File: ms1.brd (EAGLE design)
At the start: 100 x 100 mm, 123 parts, among them IC1 MAX3232EUE, J1 POWERPOLE_POWER25A, J10 RS485, J11 I2C, J12 TTL_SERIAL, J13 Radio, J14 RS232, J2 RAIN, J3 ADC1, J4 ON, J5 D1, J6 D2, J7 ADC2, J8 LED-EN, Q1 DMG6602SVT, Q2 DMG6602SVT, Q3 DMG6602SVT, Q4 DMG6602SVT, U1 LT1934ES6TRMPBF, U2 LT1934ES6TRMPBF, U3 DS3231SN, U4 ISL3179EIBZ, X1 KUSBVX-BS1N

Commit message: As submitted to hackvana
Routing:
- net RS485_P: track 18.1 -> 10.8 mm, vias 0 -> 1
- net RS485_N: track 17.7 -> 10.5 mm
- net GND: vias 18 -> 21
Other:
- board text added: "GMB"
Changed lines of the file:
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@@
 <setting verticaltext="up"/>
 </settings>
-<grid distance="5" unitdist="mil" unit="mil" style="lines" multiple="1" display="yes" altdistance="1" altunitdist="mil" altunit="mil"/>
+<grid distance="20" unitdist="mil" unit="mil" style="lines" multiple="1" display="yes" altdistance="1" altunitdist="mil" altunit="mil"/>
 <layers>
 <layer number="1" name="Top" color="4" fill="1" visible="yes" active="yes"/>
@@
 <text x="2.794" y="0.381" size="1.778" layer="25">PJB</text>
 <text x="9.652" y="0.254" size="1.778" layer="25">TW</text>
+<text x="14.859" y="0.254" size="1.778" layer="25">GMB</text>
 </plain>
 <attributes>
@@
 </class>
 <class number="2" name="rs485" width="0.3048" drill="0.3556">
-<clearance class="2" value="0.1524"/>
+<clearance class="2" value="0.3048"/>
 </class>
 </classes>
-<designrules name="Hackvana">
+<designrules name="Hackvana *">
 <description language="de">&lt;b&gt;EAGLE Design Rules&lt;/b&gt;
 &lt;p&gt;
@@
 <param name="mlMinStopFrame" value="2mil"/>
 <param name="mlMaxStopFrame" value="2mil"/>
-<param name="mlMinCreamFrame" value="0mil"/>
-<param name="mlMaxCreamFrame" value="0mil"/>
+<param name="mlMinCreamFrame" value="0.15mm"/>
+<param name="mlMaxCreamFrame" value="0.15mm"/>
 <param name="mlViaStopLimit" value="100mil"/>
 <param name="srRoundness" value="0"/>
@@
 <via x="6.604" y="33.528" extent="1-16" drill="0.4826" shape="square"/>
 <via x="64.897" y="18.161" extent="1-16" drill="0.4826" shape="square"/>
+<via x="61.976" y="32.385" extent="1-16" drill="0.4826" shape="square"/>
+<via x="87.503" y="76.581" extent="1-16" drill="0.4826" shape="square"/>
+<via x="67.691" y="86.995" extent="1-16" drill="0.4826" shape="square"/>
 </signal>
 <signal name="VCC">
@@
 <via x="11.303" y="2.667" extent="1-16" drill="0.6" shape="square"/>
 <via x="47.244" y="2.667" extent="1-16" drill="0.6" shape="square"/>
-<via x="48.514" y="34.163" extent="1-16" drill="0.6" shape="square"/>
+<via x="48.514" y="33.655" extent="1-16" drill="0.6" shape="square"/>
 <via x="10.795" y="37.465" extent="1-16" drill="0.6" shape="square"/>
 <via x="41.021" y="10.287" extent="1-16" drill="0.6" shape="square"/>
 <via x="17.145" y="18.796" extent="1-16" drill="0.6" shape="square"/>
+<via x="26.035" y="37.465" extent="1-16" drill="0.6" shape="square"/>
+<via x="33.655" y="37.465" extent="1-16" drill="0.6" shape="square"/>
+<via x="18.415" y="33.655" extent="1-16" drill="0.6" shape="square"/>
+<via x="26.035" y="33.655" extent="1-16" drill="0.6" shape="square"/>
+<via x="33.655" y="33.655" extent="1-16" drill="0.6" shape="square"/>
+<via x="45.085" y="33.655" extent="1-16" drill="0.6" shape="square"/>
+<via x="22.225" y="22.225" extent="1-16" drill="0.6" shape="square"/>
+<via x="29.845" y="22.225" extent="1-16" drill="0.6" shape="square"/>
+<via x="37.465" y="22.225" extent="1-16" drill="0.6" shape="square"/>
+<via x="22.225" y="18.415" extent="1-16" drill="0.6" shape="square"/>
+<via x="29.845" y="18.415" extent="1-16" drill="0.6" shape="square"/>
+<via x="37.465" y="18.415" extent="1-16" drill="0.6" shape="square"/>
+<via x="22.225" y="14.605" extent="1-16" drill="0.6" shape="square"/>
+<via x="29.845" y="14.605" extent="1-16" drill="0.6" shape="square"/>
+<via x="37.465" y="14.605" extent="1-16" drill="0.6" shape="square"/>
+<via x="22.225" y="10.795" extent="1-16" drill="0.6" shape="square"/>
+<via x="29.845" y="10.795" extent="1-16" drill="0.6" shape="square"/>
+<via x="22.225" y="6.985" extent="1-16" drill="0.6" shape="square"/>
+<via x="29.845" y="6.985" extent="1-16" drill="0.6" shape="square"/>
+<via x="37.465" y="6.985" extent="1-16" drill="0.6" shape="square"/>
+<via x="22.225" y="3.175" extent="1-16" drill="0.6" shape="square"/>
+<via x="29.845" y="3.175" extent="1-16" drill="0.6" shape="square"/>
+<via x="37.465" y="3.175" extent="1-16" drill="0.6" shape="square"/>
+<via x="44.958" y="27.051" extent="1-16" drill="0.6" shape="square"/>
+<via x="48.514" y="27.051" extent="1-16" drill="0.6" shape="square"/>
+<via x="44.958" y="25.019" extent="1-16" drill="0.6" shape="square"/>
+<via x="42.926" y="33.655" extent="1-16" drill="0.6" shape="square"/>
+<via x="42.926" y="27.051" extent="1-16" drill="0.6" shape="square"/>
+<via x="42.926" y="25.019" extent="1-16" drill="0.6" shape="square"/>
+<via x="10.795" y="30.607" extent="1-16" drill="0.6" shape="square"/>
+<via x="10.795" y="28.067" extent="1-16" drill="0.6" shape="square"/>
+<via x="10.795" y="25.527" extent="1-16" drill="0.6" shape="square"/>
+<via x="18.415" y="30.607" extent="1-16" drill="0.6" shape="square"/>
+<via x="18.415" y="28.067" extent="1-16" drill="0.6" shape="square"/>
+<via x="18.415" y="25.527" extent="1-16" drill="0.6" shape="square"/>
+<via x="26.035" y="30.607" extent="1-16" drill="0.6" shape="square"/>
+<via x="26.035" y="28.067" extent="1-16" drill="0.6" shape="square"/>
+<via x="26.035" y="25.527" extent="1-16" drill="0.6" shape="square"/>
+<via x="33.655" y="30.607" extent="1-16" drill="0.6" shape="square"/>
+<via x="33.655" y="28.067" extent="1-16" drill="0.6" shape="square"/>
+<via x="33.655" y="25.527" extent="1-16" drill="0.6" shape="square"/>
+<via x="18.3642" y="37.465" extent="1-16" drill="0.6" shape="square"/>
+<via x="10.795" y="33.655" extent="1-16" drill="0.6" shape="square"/>
 </signal>
 <signal name="N$24">
@@
 <contactref element="U4" pad="7"/>
 <contactref element="J10" pad="2"/>
-<wire x1="89.916" y1="15.4432" x2="89.916" y2="14.3764" width="0.3048" layer="1"/>
-<wire x1="89.916" y1="14.3764" x2="89.5096" y2="13.97" width="0.3048" layer="1"/>
-<wire x1="89.5096" y1="6.7056" x2="89.5096" y2="8.919475" width="0.3048" layer="1"/>
-<wire x1="89.5096" y1="8.919475" x2="89.8525" y2="9.262375" width="0.3048" layer="1" curve="-90"/>
-<wire x1="89.8525" y1="9.262375" x2="91.37581875" y2="9.262375" width="0.3048" layer="1"/>
-<wire x1="91.37581875" y1="9.262375" x2="91.71871875" y2="9.605275" width="0.3048" layer="1" curve="90"/>
-<wire x1="91.71871875" y1="9.605275" x2="91.71871875" y2="9.69705" width="0.3048" layer="1"/>
-<wire x1="91.71871875" y1="9.69705" x2="91.37581875" y2="10.03995" width="0.3048" layer="1" curve="90"/>
-<wire x1="91.37581875" y1="10.03995" x2="89.8525" y2="10.03995" width="0.3048" layer="1"/>
-<wire x1="89.8525" y1="10.03995" x2="89.5096" y2="10.38285" width="0.3048" layer="1" curve="-90"/>
-<wire x1="89.5096" y1="10.38285" x2="89.5096" y2="10.474625" width="0.3048" layer="1"/>
-<wire x1="89.5096" y1="10.474625" x2="89.8525" y2="10.817525" width="0.3048" layer="1" curve="-90"/>
-<wire x1="89.8525" y1="10.817525" x2="91.37581875" y2="10.817525" width="0.3048" layer="1"/>
-<wire x1="91.37581875" y1="10.817525" x2="91.71871875" y2="11.160425" width="0.3048" layer="1" curve="90"/>
-<wire x1="91.71871875" y1="11.160425" x2="91.71871875" y2="11.2522" width="0.3048" layer="1"/>
-<wire x1="91.71871875" y1="11.2522" x2="91.37581875" y2="11.5951" width="0.3048" layer="1" curve="90"/>
-<wire x1="91.37581875" y1="11.5951" x2="89.8525" y2="11.5951" width="0.3048" layer="1"/>
-<wire x1="89.8525" y1="11.5951" x2="89.5096" y2="11.938" width="0.3048" layer="1" curve="-90"/>
-<wire x1="89.5096" y1="11.938" x2="89.5096" y2="13.97" width="0.3048" layer="1"/>
-<wire x1="89.5096" y1="6.7056" x2="88.392" y2="5.588" width="0.3048" layer="1"/>
+<wire x1="89.916" y1="11.176" x2="89.916" y2="15.4432" width="0.3048" layer="1"/>
+<wire x1="89.916" y1="11.176" x2="88.392" y2="9.652" width="0.3048" layer="1"/>
+<wire x1="88.392" y1="9.652" x2="88.392" y2="5.588" width="0.3048" layer="1"/>
 </signal>
 <signal name="TTL_TX">
@@
 <contactref element="U4" pad="6"/>
 <contactref element="J10" pad="3"/>
-<wire x1="88.646" y1="15.4432" x2="88.646" y2="14.3764" width="0.3048" layer="1"/>
-<wire x1="88.646" y1="14.3764" x2="89.0524" y2="13.97" width="0.3048" layer="1"/>
-<wire x1="89.0524" y1="8.0264" x2="89.0524" y2="13.97" width="0.3048" layer="1"/>
-<wire x1="89.0524" y1="8.0264" x2="88.646" y2="7.62" width="0.3048" layer="1"/>
-<wire x1="88.646" y1="7.62" x2="88.011" y2="7.62" width="0.3048" layer="1"/>
-<wire x1="88.011" y1="7.62" x2="87.249" y2="6.858" width="0.3048" layer="1"/>
-<wire x1="87.249" y1="6.858" x2="87.249" y2="4.191" width="0.3048" layer="1"/>
-<wire x1="87.249" y1="4.191" x2="87.884" y2="3.556" width="0.3048" layer="1"/>
-<wire x1="87.884" y1="3.556" x2="90.297" y2="3.556" width="0.3048" layer="1"/>
-<wire x1="90.297" y1="3.556" x2="90.932" y2="4.191" width="0.3048" layer="1"/>
-<wire x1="90.932" y1="4.191" x2="90.932" y2="5.588" width="0.3048" layer="1"/>
+<wire x1="88.646" y1="15.4432" x2="88.646" y2="11.684" width="0.3048" layer="1"/>
+<via x="88.646" y="11.684" extent="1-16" drill="0.3556"/>
+<wire x1="88.646" y1="11.684" x2="88.646" y2="11.43" width="0.3048" layer="16"/>
+<wire x1="88.646" y1="11.43" x2="90.932" y2="9.144" width="0.3048" layer="16"/>
+<wire x1="90.932" y1="9.144" x2="90.932" y2="5.588" width="0.3048" layer="16"/>
 </signal>
 <signal name="ADC_3V3">

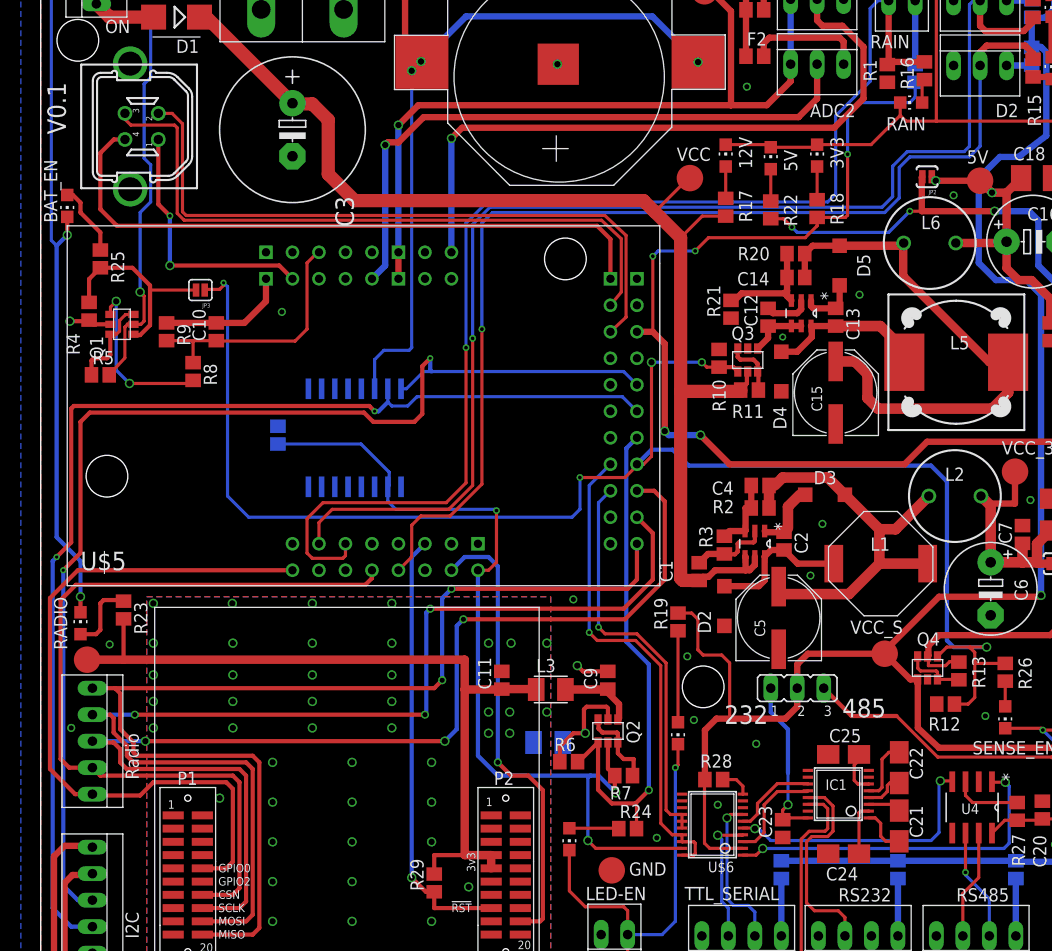
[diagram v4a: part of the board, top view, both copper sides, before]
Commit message: fixes #2 now has rs483 termination resistor
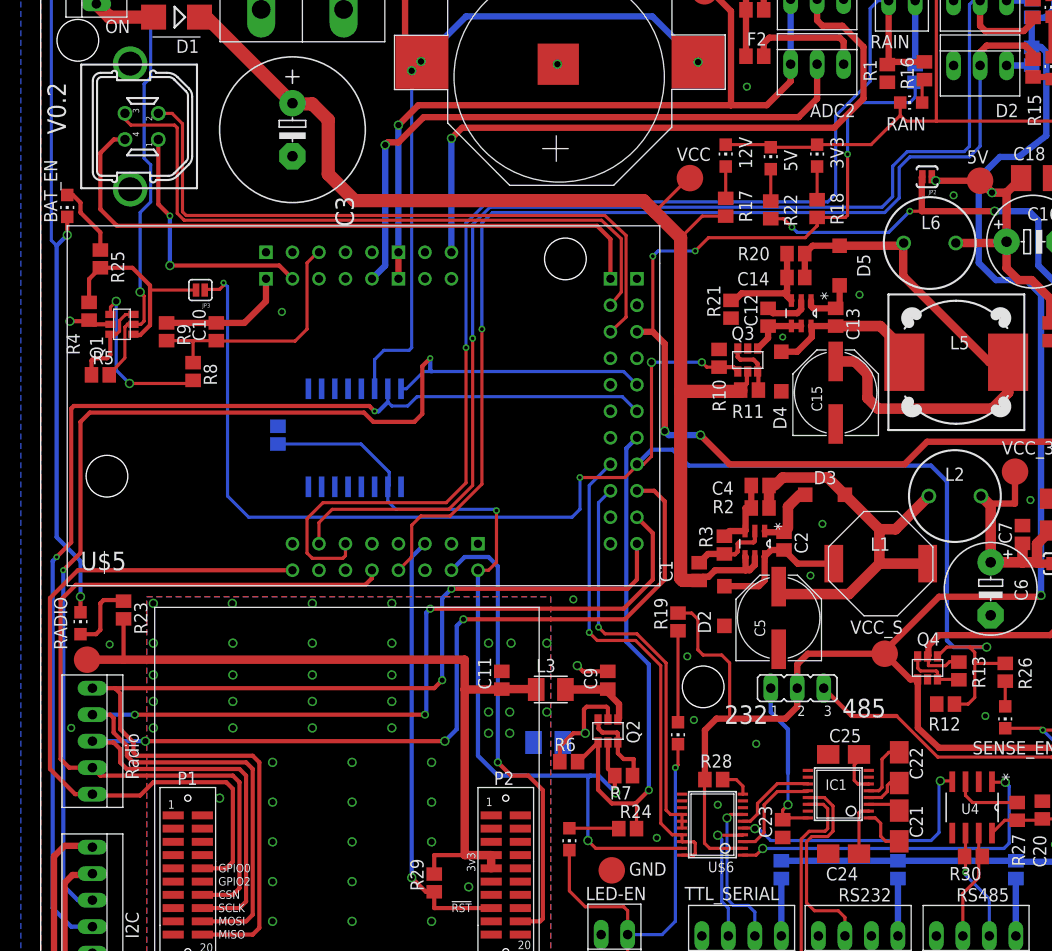
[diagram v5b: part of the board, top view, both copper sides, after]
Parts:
- added R30: 120, resistor:R0805
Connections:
- net RS485_N: now also R30.1
- net RS485_P: now also R30.2
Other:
- board text added: "V0.2"
- board text removed: "V0.1"
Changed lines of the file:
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@@
 <text x="76.835" y="26.543" size="1.778" layer="25">485</text>
 <text x="9.779" y="97.028" size="1.778" layer="25">MS1</text>
-<text x="2.413" y="82.423" size="1.778" layer="25" rot="R90">V0.1</text>
+<text x="2.413" y="82.423" size="1.778" layer="25" rot="R90">V0.2</text>
 <text x="2.794" y="0.381" size="1.778" layer="25">PJB</text>
 <text x="9.652" y="0.254" size="1.778" layer="25">TW</text>
@@
 <attribute name="NAME" x="96.012" y="93.726" size="1.27" layer="26" rot="MR90"/>
 </element>
+<element name="R30" library="resistor" package="R0805" value="120" x="89.408" y="13.208" rot="R180"/>
 </elements>
 <signals>
@@
 <contactref element="U4" pad="7"/>
 <contactref element="J10" pad="2"/>
-<wire x1="89.916" y1="11.176" x2="89.916" y2="15.4432" width="0.3048" layer="1"/>
+<wire x1="89.916" y1="11.176" x2="89.916" y2="13.208" width="0.3048" layer="1"/>
+<wire x1="89.916" y1="13.208" x2="89.916" y2="15.4432" width="0.3048" layer="1"/>
 <wire x1="89.916" y1="11.176" x2="88.392" y2="9.652" width="0.3048" layer="1"/>
 <wire x1="88.392" y1="9.652" x2="88.392" y2="5.588" width="0.3048" layer="1"/>
+<contactref element="R30" pad="1"/>
+<wire x1="90.258" y1="13.208" x2="89.916" y2="13.208" width="0.3048" layer="1"/>
 </signal>
 <signal name="TTL_TX">
@@
 <contactref element="U4" pad="6"/>
 <contactref element="J10" pad="3"/>
-<wire x1="88.646" y1="15.4432" x2="88.646" y2="11.684" width="0.3048" layer="1"/>
+<wire x1="88.646" y1="15.4432" x2="88.646" y2="13.208" width="0.3048" layer="1"/>
 <via x="88.646" y="11.684" extent="1-16" drill="0.3556"/>
+<wire x1="88.646" y1="13.208" x2="88.646" y2="11.684" width="0.3048" layer="1"/>
 <wire x1="88.646" y1="11.684" x2="88.646" y2="11.43" width="0.3048" layer="16"/>
 <wire x1="88.646" y1="11.43" x2="90.932" y2="9.144" width="0.3048" layer="16"/>
 <wire x1="90.932" y1="9.144" x2="90.932" y2="5.588" width="0.3048" layer="16"/>
+<contactref element="R30" pad="2"/>
+<wire x1="88.558" y1="13.208" x2="88.646" y2="13.208" width="0.3048" layer="1"/>
 </signal>
 <signal name="ADC_3V3">

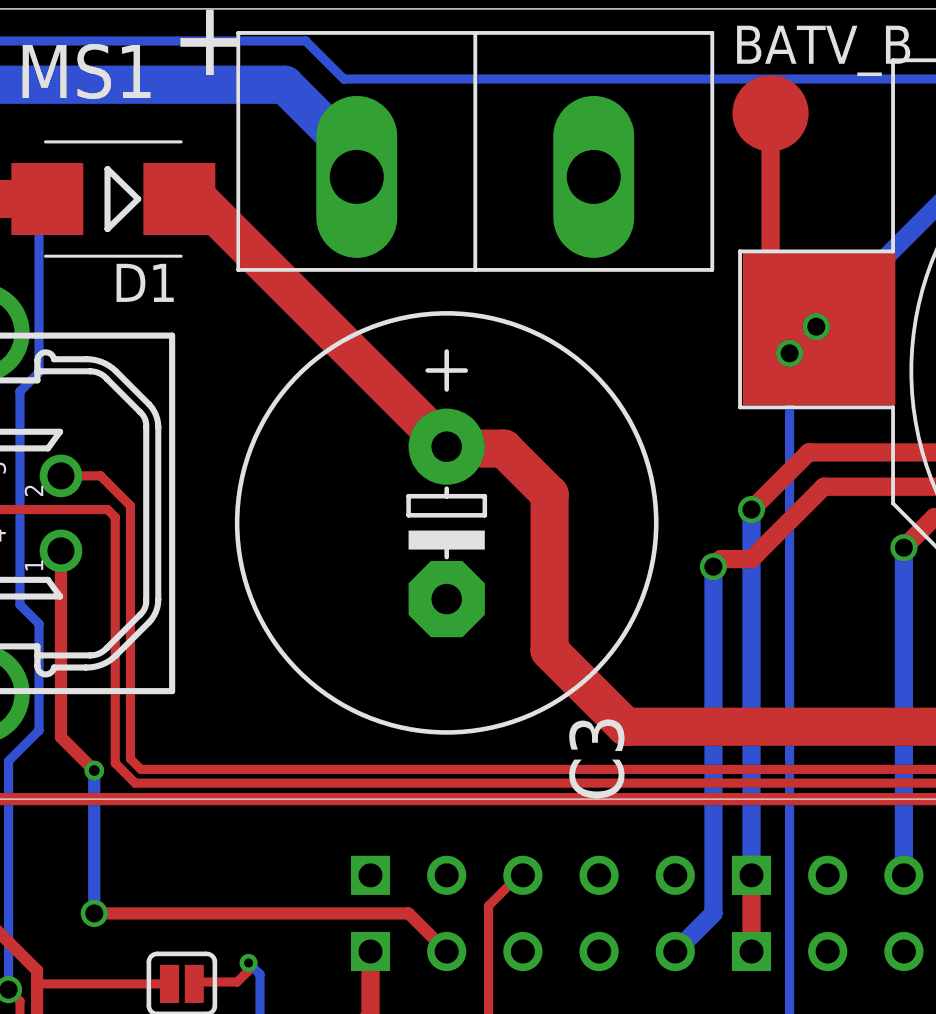
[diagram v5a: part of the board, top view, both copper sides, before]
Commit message: fixes #7 now has gnd link header
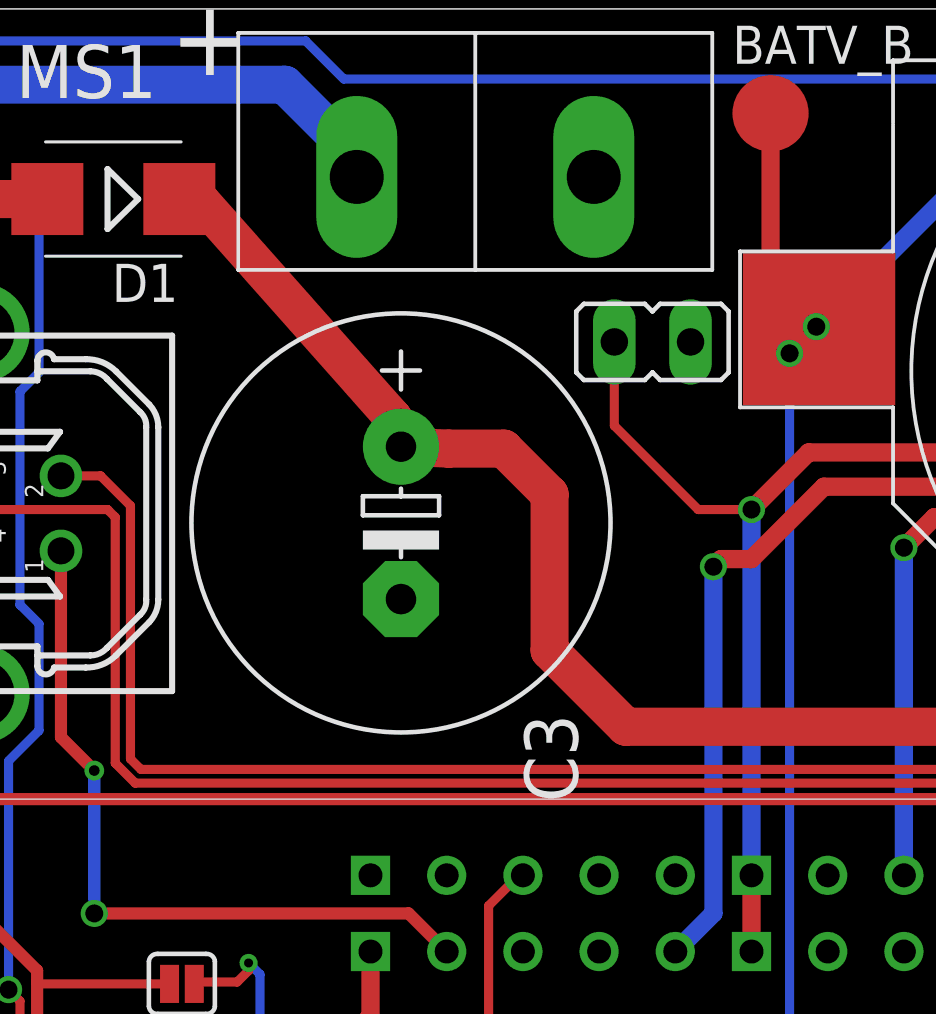
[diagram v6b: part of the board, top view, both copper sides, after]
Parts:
- added JP5: GND-LINK, jumper:JP1
- moved C3 1.52 mm to (22.6, 82.9)
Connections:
- net AGND: now also JP5.2
- net GND: now also JP5.1
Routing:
- net AGND: track 86.9 -> 95.5 mm
- net VCC: track 118.6 -> 120.2 mm
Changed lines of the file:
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@@
 <layer number="25" name="tNames" color="7" fill="1" visible="yes" active="yes"/>
 <layer number="26" name="bNames" color="7" fill="1" visible="yes" active="yes"/>
-<layer number="27" name="tValues" color="7" fill="1" visible="no" active="yes"/>
+<layer number="27" name="tValues" color="7" fill="1" visible="yes" active="yes"/>
 <layer number="28" name="bValues" color="7" fill="1" visible="no" active="yes"/>
 <layer number="29" name="tStop" color="7" fill="3" visible="no" active="yes"/>
@@
 <attribute name="VALUE" x="8.5725" y="93.4085" size="1.27" layer="25" ratio="10" rot="R180"/>
 </element>
-<element name="C3" library="rcl" package="E5-13" value="2200uF" x="24.13" y="82.8675" rot="R270"/>
+<element name="C3" library="rcl" package="E5-13" value="2200uF" x="22.606" y="82.8675" rot="R270"/>
 <element name="Q4" library="farnell-parts" package="TSOT26" value="DMG6602SVT" x="86.36" y="30.48" smashed="yes" rot="R180">
 <attribute name="NAME" x="86.201" y="34.687" size="1.27" layer="25" rot="R180"/>
@@
 </element>
 <element name="R30" library="resistor" package="R0805" value="120" x="89.408" y="13.208" rot="R180"/>
+<element name="JP5" library="jumper" package="JP1" value="GND-LINK" x="30.988" y="88.9" smashed="yes" rot="R90">
+<attribute name="VALUE" x="38.1" y="85.725" size="1.27" layer="27" ratio="10" rot="R180"/>
+</element>
 </elements>
 <signals>
@@
 <via x="87.503" y="76.581" extent="1-16" drill="0.4826" shape="square"/>
 <via x="67.691" y="86.995" extent="1-16" drill="0.4826" shape="square"/>
+<contactref element="JP5" pad="1"/>
 </signal>
 <signal name="VCC">
@@
 <contactref element="D1" pad="C"/>
 <wire x1="15.2175" y1="93.6625" x2="15.875" y2="93.6625" width="1.27" layer="1"/>
-<wire x1="15.875" y1="93.6625" x2="24.13" y2="85.4075" width="1.27" layer="1"/>
+<wire x1="15.875" y1="93.6625" x2="22.352" y2="86.36" width="1.27" layer="1"/>
+<wire x1="22.352" y1="86.36" x2="22.352" y2="84.8995" width="1.27" layer="1"/>
+<wire x1="22.352" y1="84.8995" x2="22.606" y2="85.4075" width="1.27" layer="1"/>
 <wire x1="63.119" y1="39.663" x2="63.461" y2="40.005" width="0.6096" layer="1"/>
 <wire x1="63.461" y1="40.005" x2="64.008" y2="40.005" width="0.6096" layer="1"/>
@@
 <wire x1="27.559" y1="83.82" x2="26.035" y2="85.344" width="1.27" layer="1"/>
 <wire x1="26.035" y1="85.344" x2="24.1935" y2="85.344" width="1.27" layer="1"/>
-<wire x1="24.1935" y1="85.344" x2="24.13" y2="85.4075" width="1.27" layer="1"/>
+<wire x1="24.1935" y1="85.344" x2="22.606" y2="85.4075" width="1.27" layer="1"/>
 <wire x1="63.119" y1="39.663" x2="61.556" y2="39.663" width="1.27" layer="1"/>
 <wire x1="61.556" y1="39.663" x2="61.341" y2="39.878" width="1.27" layer="1"/>
@@
 <wire x1="64.262" y1="96.139" x2="66.167" y2="94.234" width="0.6096" layer="1"/>
 <wire x1="66.167" y1="94.234" x2="66.167" y2="85.217" width="0.6096" layer="1"/>
+<contactref element="JP5" pad="2"/>
+<wire x1="29.718" y1="88.9" x2="29.718" y2="86.106" width="0.3048" layer="1"/>
+<wire x1="29.718" y1="86.106" x2="32.512" y2="83.312" width="0.3048" layer="1"/>
+<wire x1="32.512" y1="83.312" x2="34.29" y2="83.312" width="0.3048" layer="1"/>
 </signal>
 <signal name="SCL">
